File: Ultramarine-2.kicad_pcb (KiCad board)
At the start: 2 copper layers, 135 x 122.8 mm, 116 parts, among them J1 OLED, J2 TRRS, J3 Flexible LED 3V, J4 Flexible LED GND, SW1 SW_Push, SW10 SW_Push, SW11 SW_Push, SW12 SW_Push, SW13 SW_Push, SW14 SW_Push, SW15 SW_Push, SW16 SW_Push, SW17 SW_Push, SW18 SW_Push, SW19 SW_Push, SW2 SW_Push, SW20 SW_Push, SW21 SW_Push, SW22 SW_Push, SW23 SW_Push, SW24 SW_Push, SW25 SW_Push, SW26 SW_Push, SW27 SW_Push, SW28 Extra, SW29 SW_Push, SW3 SW_Push, SW30 SW_Push, SW31 SW_Push, SW32 RotaryEncoder_Switch, SW33 Reset, SW34 Slide, SW4 SW_Push, SW5 SW_Push, SW6 SW_Push, SW7 SW_Push, SW8 SW_Push, SW9 SW_Push

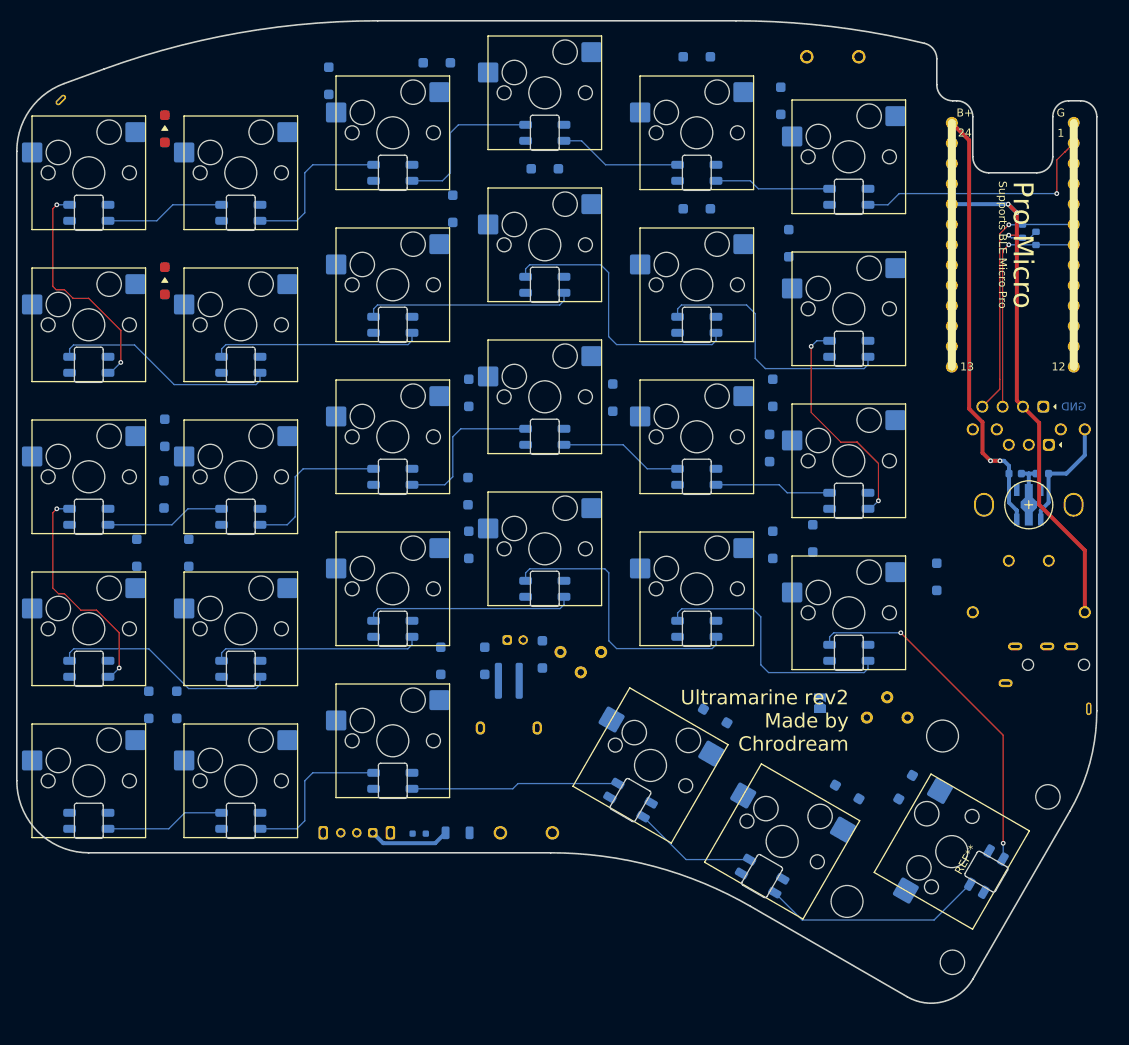
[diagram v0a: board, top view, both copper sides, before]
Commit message: starts build left hand
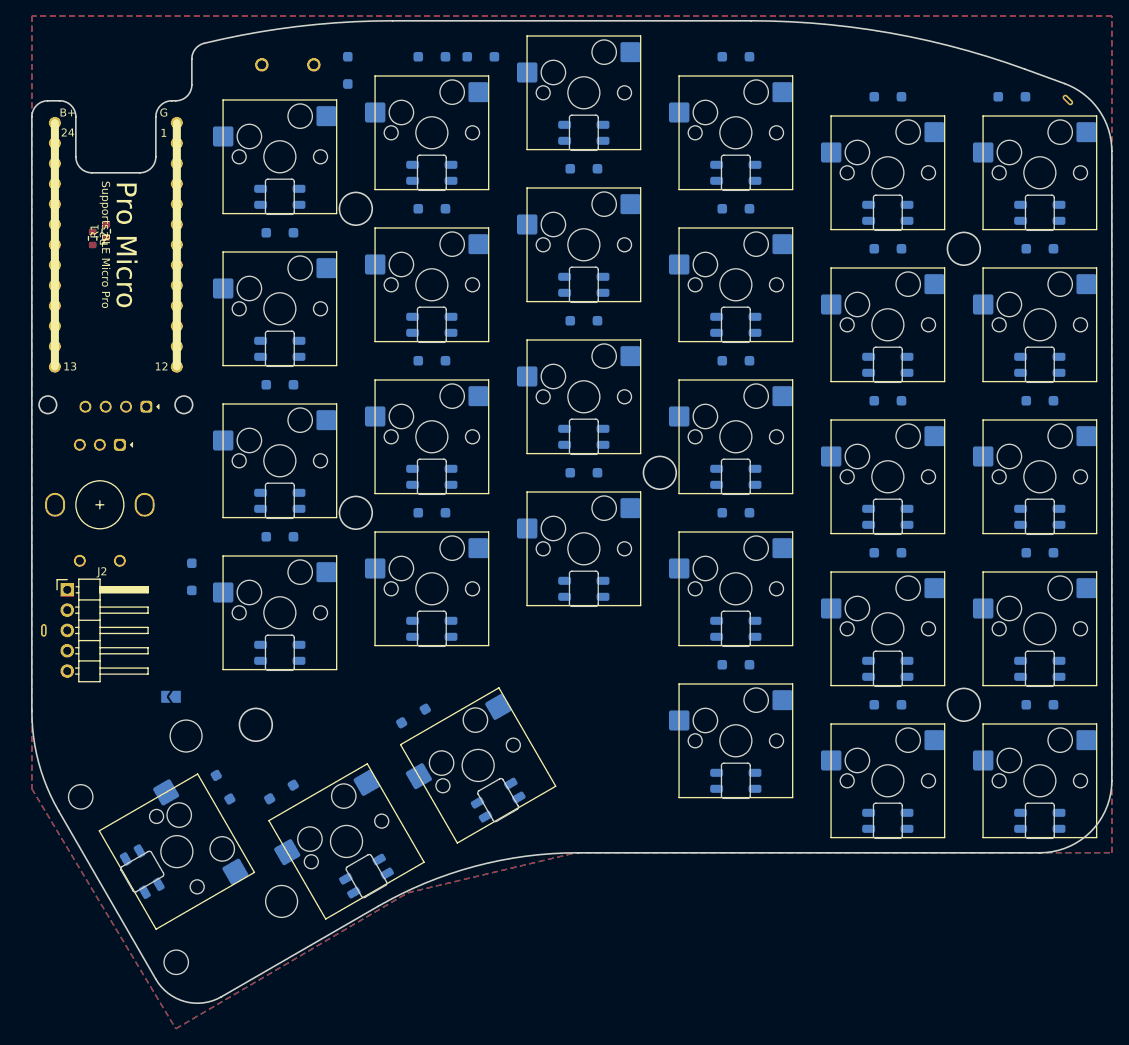
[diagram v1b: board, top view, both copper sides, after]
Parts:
- removed BT1: Qi Charging Unit, Ultramarine-2:Micro_USB_Charging
- removed BT2: LiPo, Ultramarine-2:Battery
- removed C1: 0.33u, Capacitor_SMD:C_0603_1608Metric
- removed C2: 2.2u, Capacitor_SMD:C_0603_1608Metric
- removed the D29 at (144.5, 111.0)
- removed D63: D, Ultramarine-2:SOD-123
- removed D64: Power (WH), Ultramarine-2:LED1608
- removed F1: 350mA, Ultramarine-2:MF-NSMF
- removed J3: Flexible LED 3V, Ultramarine-2:PTH_Flex_LED
- removed RV1, RV2: 10K, Ultramarine-2:R_variable
- removed the SW28 at (149.7, 132.5)
- removed SW34: Slide, Ultramarine-2:SK-12D11VG3
- removed U2: ~, Package_TO_SOT_SMD:SOT-89-5
- removed U3: ~, Ultramarine-2:TP4056
- added Je: Flex LED 3V, Ultramarine-2:PTH_Flex_LED, B.Cu at (89.4, 107.2)
- D1, D7, REF**: moved to B.Cu
- J2: value TRRS -> Generic_connector; footprint Ultramarine-2:MJ-4PP-9 -> Connector_PinHeader_2.54mm:PinHeader_1x05_P2.54mm_Horizontal; moved to F.Cu
- J4: value Flexible LED GND -> Flex LED GND; moved to B.Cu
- R1, R2: moved to F.Cu
- moved J2 129.0 mm to (92.3, 102.1), turned to 0 degrees
- moved J4 125.9 mm to (217.4, 40.9), turned to 45 degrees
- moved D32 118.9 mm to (213.9, 55.0)
- moved D38 118.9 mm to (213.9, 74.0)
- moved D44 118.9 mm to (213.9, 93.0)
- moved D50 118.9 mm to (213.9, 112.0)
- moved D56 118.9 mm to (213.9, 131.0)
- moved SW1 118.9 mm to (213.9, 50.0)
- moved SW13 118.9 mm to (213.9, 88.0)
- moved SW19 118.9 mm to (213.9, 107.0)
- moved SW25 118.9 mm to (213.9, 126.0)
- moved SW7 118.9 mm to (213.9, 69.0)
- moved R2 117.9 mm to (95.5, 58.2)
- moved SW31 116.1 mm to (96.4, 91.5)
- moved R1 114.5 mm to (97.2, 57.3)
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- renumbered D30 to D29, D31 to D30, D32 to D31, D33 to D32, D34 to D33, D35 to D34, D36 to D35, D37 to D36, D38 to D37, D39 to D38, D40 to D39, D41 to D40, D42 to D41, D43 to D42, D44 to D43, D45 to D44, D46 to D45, D47 to D46, D48 to D47, D49 to D48, D50 to D49, D51 to D50, D52 to D51, D53 to D52, D54 to D53, D55 to D54, D56 to D55, D57 to D56, D58 to D57, D59 to D58, D60 to D59, D61 to D60, D62 to D61, SW29 to SW28, SW30 to SW29, SW31 to SW30, SW32 to SW31, SW33 to SW32
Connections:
- J2 pad 2: GND -> /Bat+
- J2 pad 3: /data -> Net-(J2-Pin_3)
- J2 pad 4: unconnected-(J2-Pin_4-Pad4) -> /data
- SW1 pad 1: /C0 -> Net-(D1-A)
- SW1 pad 2: Net-(D1-A) -> /C0
- SW10 pad 1: /C3 -> Net-(D10-A)
- SW10 pad 2: Net-(D10-A) -> /C3
- SW11 pad 1: /C4 -> Net-(D11-A)
- SW11 pad 2: Net-(D11-A) -> /C4
- SW12 pad 1: /C5 -> Net-(D12-A)
- SW12 pad 2: Net-(D12-A) -> /C5
- SW13 pad 1: /C0 -> Net-(D13-A)
- SW13 pad 2: Net-(D13-A) -> /C0
- SW14 pad 1: /C1 -> Net-(D14-A)
- SW14 pad 2: Net-(D14-A) -> /C1
- SW15 pad 1: /C2 -> Net-(D15-A)
- SW15 pad 2: Net-(D15-A) -> /C2
- SW16 pad 1: /C3 -> Net-(D16-A)
- SW16 pad 2: Net-(D16-A) -> /C3
- SW17 pad 1: /C4 -> Net-(D17-A)
- SW17 pad 2: Net-(D17-A) -> /C4
- SW18 pad 1: /C5 -> Net-(D18-A)
- SW18 pad 2: Net-(D18-A) -> /C5
- SW19 pad 1: /C0 -> Net-(D19-A)
- SW19 pad 2: Net-(D19-A) -> /C0
- SW2 pad 1: /C1 -> Net-(D2-A)
- SW2 pad 2: Net-(D2-A) -> /C1
- SW20 pad 1: /C1 -> Net-(D20-A)
- SW20 pad 2: Net-(D20-A) -> /C1
- SW21 pad 1: /C2 -> Net-(D21-A)
- SW21 pad 2: Net-(D21-A) -> /C2
- SW22 pad 1: /C3 -> Net-(D22-A)
- SW22 pad 2: Net-(D22-A) -> /C3
- SW23 pad 1: /C4 -> Net-(D23-A)
- SW23 pad 2: Net-(D23-A) -> /C4
- SW24 pad 1: /C5 -> Net-(D24-A)
- SW24 pad 2: Net-(D24-A) -> /C5
- SW25 pad 1: /C0 -> Net-(D26-A)
- SW25 pad 2: Net-(D26-A) -> /C0
- SW26 pad 1: /C1 -> Net-(D27-A)
- SW26 pad 2: Net-(D27-A) -> /C1
- SW27 pad 1: /C2 -> Net-(D28-A)
- SW27 pad 2: Net-(D28-A) -> /C2
- SW3 pad 1: /C2 -> Net-(D3-A)
- SW3 pad 2: Net-(D3-A) -> /C2
- SW4 pad 1: /C3 -> Net-(D4-A)
- SW4 pad 2: Net-(D4-A) -> /C3
- SW5 pad 1: /C4 -> Net-(D5-A)
- SW5 pad 2: Net-(D5-A) -> /C4
- SW6 pad 1: /C5 -> Net-(D6-A)
- SW6 pad 2: Net-(D6-A) -> /C5
- SW7 pad 1: /C0 -> Net-(D7-A)
- SW7 pad 2: Net-(D7-A) -> /C0
- SW8 pad 1: /C1 -> Net-(D8-A)
- SW8 pad 2: Net-(D8-A) -> /C1
- SW9 pad 1: /C2 -> Net-(D9-A)
- SW9 pad 2: Net-(D9-A) -> /C2
- U1 pad 21: +5V -> unconnected-(U1-4.3V-Pad21)
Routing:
- net +5V: track 68.4 -> 0.00 mm, vias 3 -> 0
- net /Bat+: track 55.1 -> 0.00 mm, vias 2 -> 0
- net Net-(D55-DOUT): track 43.7 -> 0.00 mm, vias 2 -> 0
- net Net-(D53-DOUT): track 35.3 -> 0.00 mm
- net Net-(D41-DOUT): track 35.0 -> 0.00 mm
- net Net-(D54-DOUT): track 33.0 -> 0.00 mm
- net Net-(D42-DOUT): track 32.8 -> 0.00 mm
- net /SDA: track 32.2 -> 0.00 mm, vias 1 -> 0
- net /LED: track 31.4 -> 0.00 mm, vias 1 -> 0
- net Net-(D32-DOUT): track 28.9 -> 0.00 mm, vias 2 -> 0
- net /SCL: track 28.7 -> 0.00 mm, vias 1 -> 0
- net Net-(D44-DOUT): track 28.6 -> 0.00 mm, vias 2 -> 0
- net Net-(D43-DOUT): track 28.3 -> 0.00 mm, vias 2 -> 0
- net Net-(D50-DOUT): track 28.3 -> 0.00 mm
- net Net-(D38-DOUT): track 28.2 -> 0.00 mm
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- added copper zone on B.Cu, net GND
- added copper zone on F.Cu, net GND
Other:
- outline, holes or cut-outs redrawn
